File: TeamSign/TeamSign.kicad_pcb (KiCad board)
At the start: 2 copper layers, 241.2 x 139.8 mm, 203 parts, among them J1 RJ45, J2 Barrel_Jack_MountingPin, Q1 BSS138, Q2 BSS138, U1 TPS563200, U2 ESP32-Devkit_C_V4

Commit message: Added reset pins back in and broke out the pins in the team control area; should be easier now.  Yay!
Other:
- board size 241.2 x 139.8 mm -> 231.1 x 135.5 mm
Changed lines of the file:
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@@
       (net 1 "GND") (pintype "passive"))
   )
-  (gr_rect (start 32 19.25) (end 273.25 159)
-    (stroke (width 0.1) (type default)) (fill none) (layer "Edge.Cuts"))
+  (gr_line (start 258.15 154.725) (end 37 154.725)
+    (stroke (width 0.1) (type default)) (layer "Edge.Cuts"))
+  (gr_line (start 32 149.725) (end 32 24.25)
+    (stroke (width 0.1) (type default)) (layer "Edge.Cuts"))
+  (gr_line (start 263.15 24.25) (end 263.15 149.725)
+    (stroke (width 0.1) (type default)) (layer "Edge.Cuts"))
+  (gr_arc (start 32 24.25) (mid 33.464466 20.714466) (end 37 19.25)
+    (stroke (width 0.1) (type default)) (layer "Edge.Cuts"))
+  (gr_arc (start 263.15 149.725) (mid 261.685534 153.260534) (end 258.15 154.725)
+    (stroke (width 0.1) (type default)) (layer "Edge.Cuts"))
+  (gr_line (start 37 19.25) (end 258.15 19.25)
+    (stroke (width 0.1) (type default)) (layer "Edge.Cuts"))
+  (gr_arc (start 258.15 19.25) (mid 261.685534 20.714466) (end 263.15 24.25)
+    (stroke (width 0.1) (type default)) (layer "Edge.Cuts"))
+  (gr_arc (start 37 154.725) (mid 33.464466 153.260534) (end 32 149.725)
+    (stroke (width 0.1) (type default)) (layer "Edge.Cuts"))
   (gr_text "888" (at 30.9499 162.5346) (layer "F.SilkS")
     (effects (font (face "DSEG7 Classic Mini") (size 70 70) (thickness 0.3) bold) (justify left bottom))

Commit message: Added power area, and started drawing pours.
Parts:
- added C87: 100nF, Capacitor_SMD:C_1206_3216Metric_Pad1.33x1.80mm_HandSolder, F.Cu at (193.9, 26.3)
- added C90: 100nF, Capacitor_SMD:C_1206_3216Metric_Pad1.33x1.80mm_HandSolder, F.Cu at (208.2, 26.3)
- added C93: 100nF, Capacitor_SMD:C_1206_3216Metric_Pad1.33x1.80mm_HandSolder, F.Cu at (222.4, 26.3)
- added C96: 100nF, Capacitor_SMD:C_1206_3216Metric_Pad1.33x1.80mm_HandSolder, F.Cu at (179.7, 26.3)
- added D29: SK6812, LED_SMD:LED_SK6812_PLCC4_5.0x5.0mm_P3.2mm, F.Cu at (222.8, 33.0)
- added D30: SK6812, LED_SMD:LED_SK6812_PLCC4_5.0x5.0mm_P3.2mm, F.Cu at (208.4, 33.0)
- added D31: SK6812, LED_SMD:LED_SK6812_PLCC4_5.0x5.0mm_P3.2mm, F.Cu at (194.0, 33.0)
- added D32: SK6812, LED_SMD:LED_SK6812_PLCC4_5.0x5.0mm_P3.2mm, F.Cu at (179.6, 33.0)
- added H1: MountingHole, MountingHole:MountingHole_3.2mm_M3, F.Cu at (30.0, 20.0)
- added H2: MountingHole, MountingHole:MountingHole_3.2mm_M3, F.Cu at (260.0, 19.7)
- added H3: MountingHole, MountingHole:MountingHole_3.2mm_M3, F.Cu at (30.0, 155.0)
- added H4: MountingHole, MountingHole:MountingHole_3.2mm_M3, F.Cu at (260.0, 155.0)
- moved C998 31.2 mm to (131.6, 24.8), turned to 90 degrees
- moved C999 28.9 mm to (135.7, 24.8), turned to 90 degrees
- moved L1 27.4 mm to (152.6, 26.0)
- moved U1 25.2 mm to (143.8, 24.7)
- moved R4 23.6 mm to (68.4, 34.0), turned to 0 degrees
- moved R3 22.4 mm to (139.0, 24.8), turned to 90 degrees
- moved C899 19.6 mm to (148.7, 35.0), turned to 90 degrees
- moved R2 19.2 mm to (141.5, 30.6), turned to 180 degrees
- moved C799 17.9 mm to (146.0, 20.0)
- moved R6 16.8 mm to (57.8, 27.0), turned to 0 degrees
- moved R5 16.3 mm to (65.1, 38.0)
- moved J2 16.1 mm to (122.6, 28.8)
- moved R1 15.5 mm to (145.6, 29.4), turned to 90 degrees
- moved C898 15.1 mm to (155.8, 35.0), turned to 90 degrees
- moved Q2 13.4 mm to (57.7, 30.8)
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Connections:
- D92 pad 4: /LED Array 3/sk_output_pin -> /led_output_frontfiring
- U2 pad 26: /sk_input -> /stacklight_out
- U2 pad 27: /stacklight_out -> /sk_input
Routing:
- net +5V: track 0.00 -> 189.7 mm, vias 0 -> 5
- net +3.3V: track 0.00 -> 87.2 mm, vias 0 -> 4
- net /sk_lvl_shifted: track 0.00 -> 54.6 mm
- net /stacklight_lvl_shift: track 0.00 -> 49.4 mm
- net /stacklight_out: track 0.00 -> 45.4 mm
- net +12V: track 0.00 -> 21.7 mm
- net Net-(U1-EN): track 0.00 -> 14.2 mm, vias 0 -> 2
- net /sk_input: track 0.00 -> 12.5 mm
- net Net-(U1-VBST): track 0.00 -> 11.8 mm
- net Net-(U1-SW): track 0.00 -> 8.79 mm
- net Net-(U1-VFB): track 0.00 -> 7.12 mm
- net GND: track 0.00 -> 0.09 mm, vias 0 -> 53
- added copper zone on F.Cu, net +5V
- added copper zone on B.Cu, net GND
- added copper zone on F.Cu, net GND
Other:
- board size 231.1 x 135.5 mm -> 240 x 145 mm
- board text added: "locked"
- board text removed: "888"

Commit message: Fight with Freerouting, turns out there's a bug.  Routing by hand.
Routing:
- net +5V: track 189.7 -> 300.5 mm
- net /LED Array 1/sk_output_pin: track 0.00 -> 81.8 mm
- net /LED Array 2/sk_output_pin: track 0.00 -> 79.7 mm
- net /led_output_frontfiring: track 0.00 -> 78.8 mm, vias 0 -> 2
- net GND: track 0.09 -> 45.4 mm, vias 53 -> 61
- net +12V: track 21.7 -> 45.6 mm
- net Net-(D31-DOUT): track 0.00 -> 10.8 mm
- net Net-(D29-DOUT): track 0.00 -> 10.8 mm
- net Net-(D30-DOUT): track 0.00 -> 10.8 mm
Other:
- board text added: "888"
- board text removed: "locked"

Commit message: Mostly routed, needs side-firing cleanup.
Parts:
- moved C16 3.53 mm to (212.0, 139.8)
- turned C11 to 180 degrees
- turned C14 to 180 degrees
- turned C5 to 180 degrees
- turned C8 to 180 degrees
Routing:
- net +5V: track 300.5 -> 2683.5 mm, vias 5 -> 42
- net Net-(D24-DOUT): track 0.00 -> 59.0 mm
- net Net-(D60-DOUT): track 0.00 -> 56.7 mm
- net Net-(D88-DOUT): track 0.00 -> 54.9 mm
- net Net-(D304-DOUT): track 0.00 -> 25.5 mm, vias 0 -> 2
- net Net-(D305-DOUT): track 0.00 -> 25.2 mm
- net Net-(D302-DOUT): track 0.00 -> 24.5 mm, vias 0 -> 2
- net Net-(D303-DOUT): track 0.00 -> 22.8 mm, vias 0 -> 2
- net GND: track 45.4 -> 68.1 mm, vias 61 -> 194
- net Net-(D300-DOUT): track 0.00 -> 21.5 mm, vias 0 -> 2
- net Net-(D8-DOUT): track 0.00 -> 21.0 mm, vias 0 -> 2
- net Net-(D306-DOUT): track 0.00 -> 20.9 mm, vias 0 -> 2
- net Net-(D44-DOUT): track 0.00 -> 19.7 mm, vias 0 -> 2
- net Net-(D84-DOUT): track 0.00 -> 19.5 mm
- net Net-(D72-DOUT): track 0.00 -> 19.5 mm
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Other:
- board text added: "locked"
- board text removed: "888"

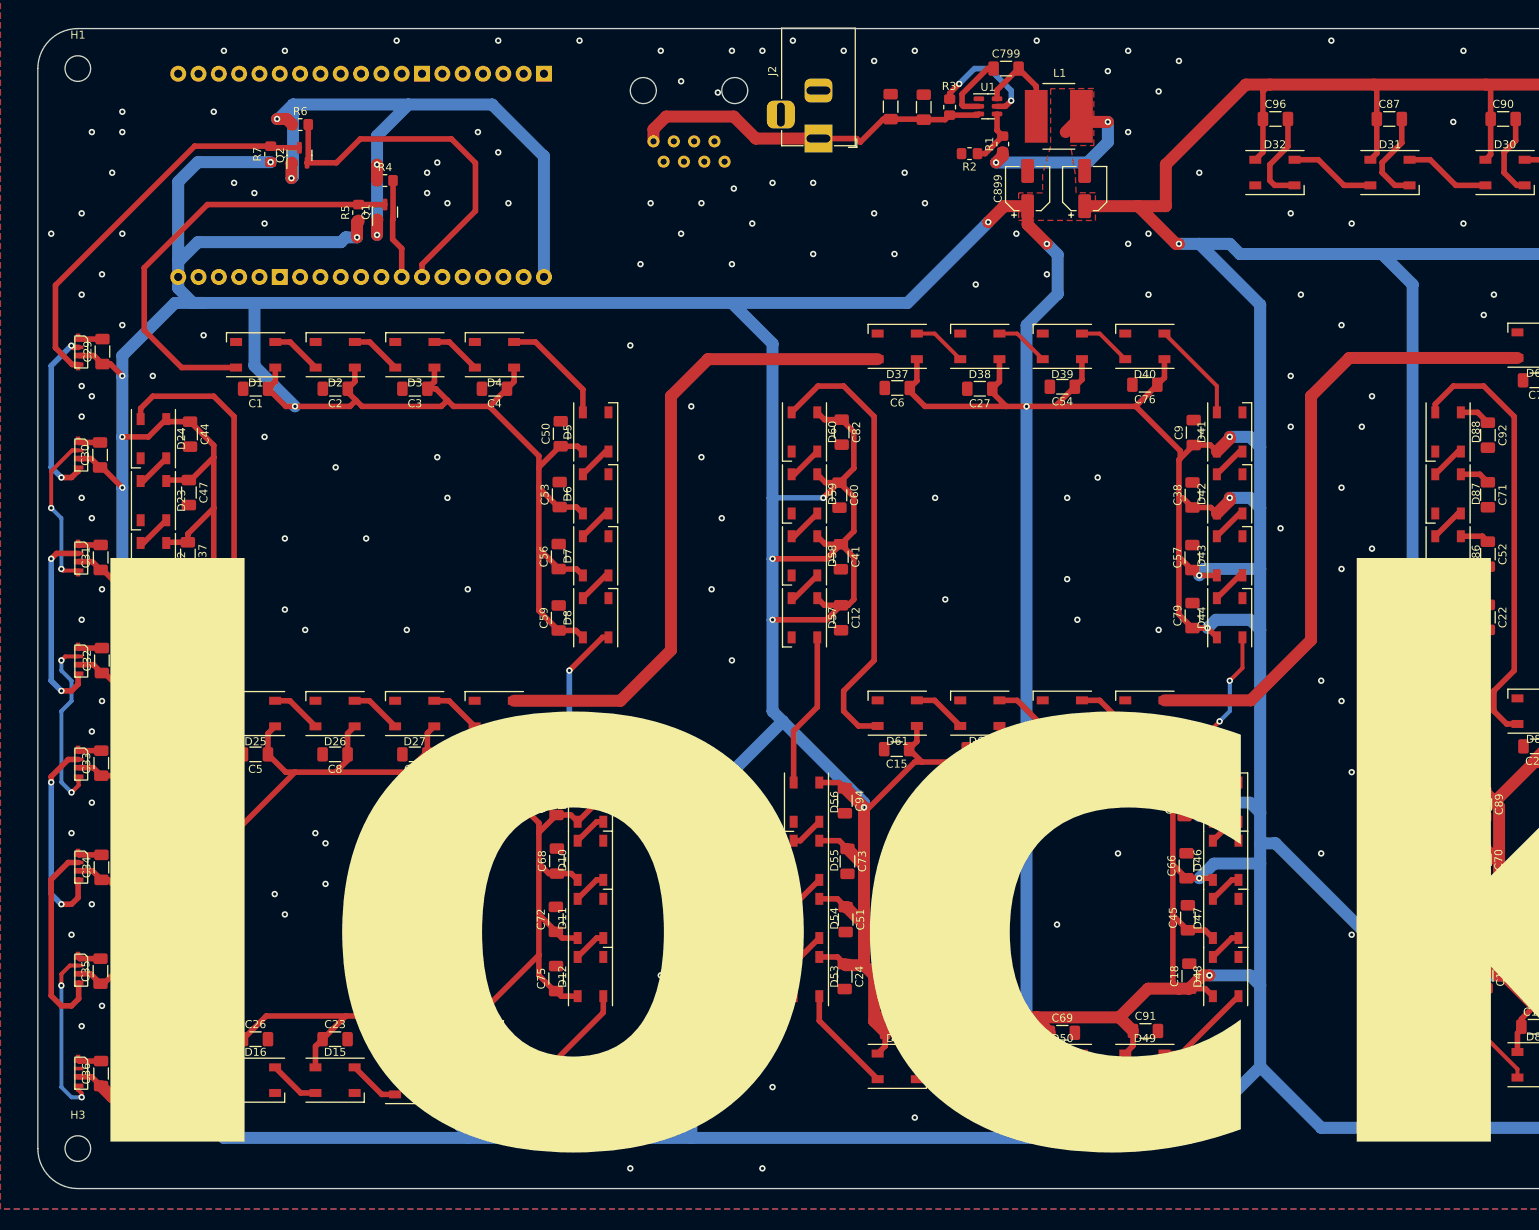
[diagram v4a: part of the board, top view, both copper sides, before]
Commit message: Changed thermal relief style, updated LEDs, seem to have worked?  idk, yay
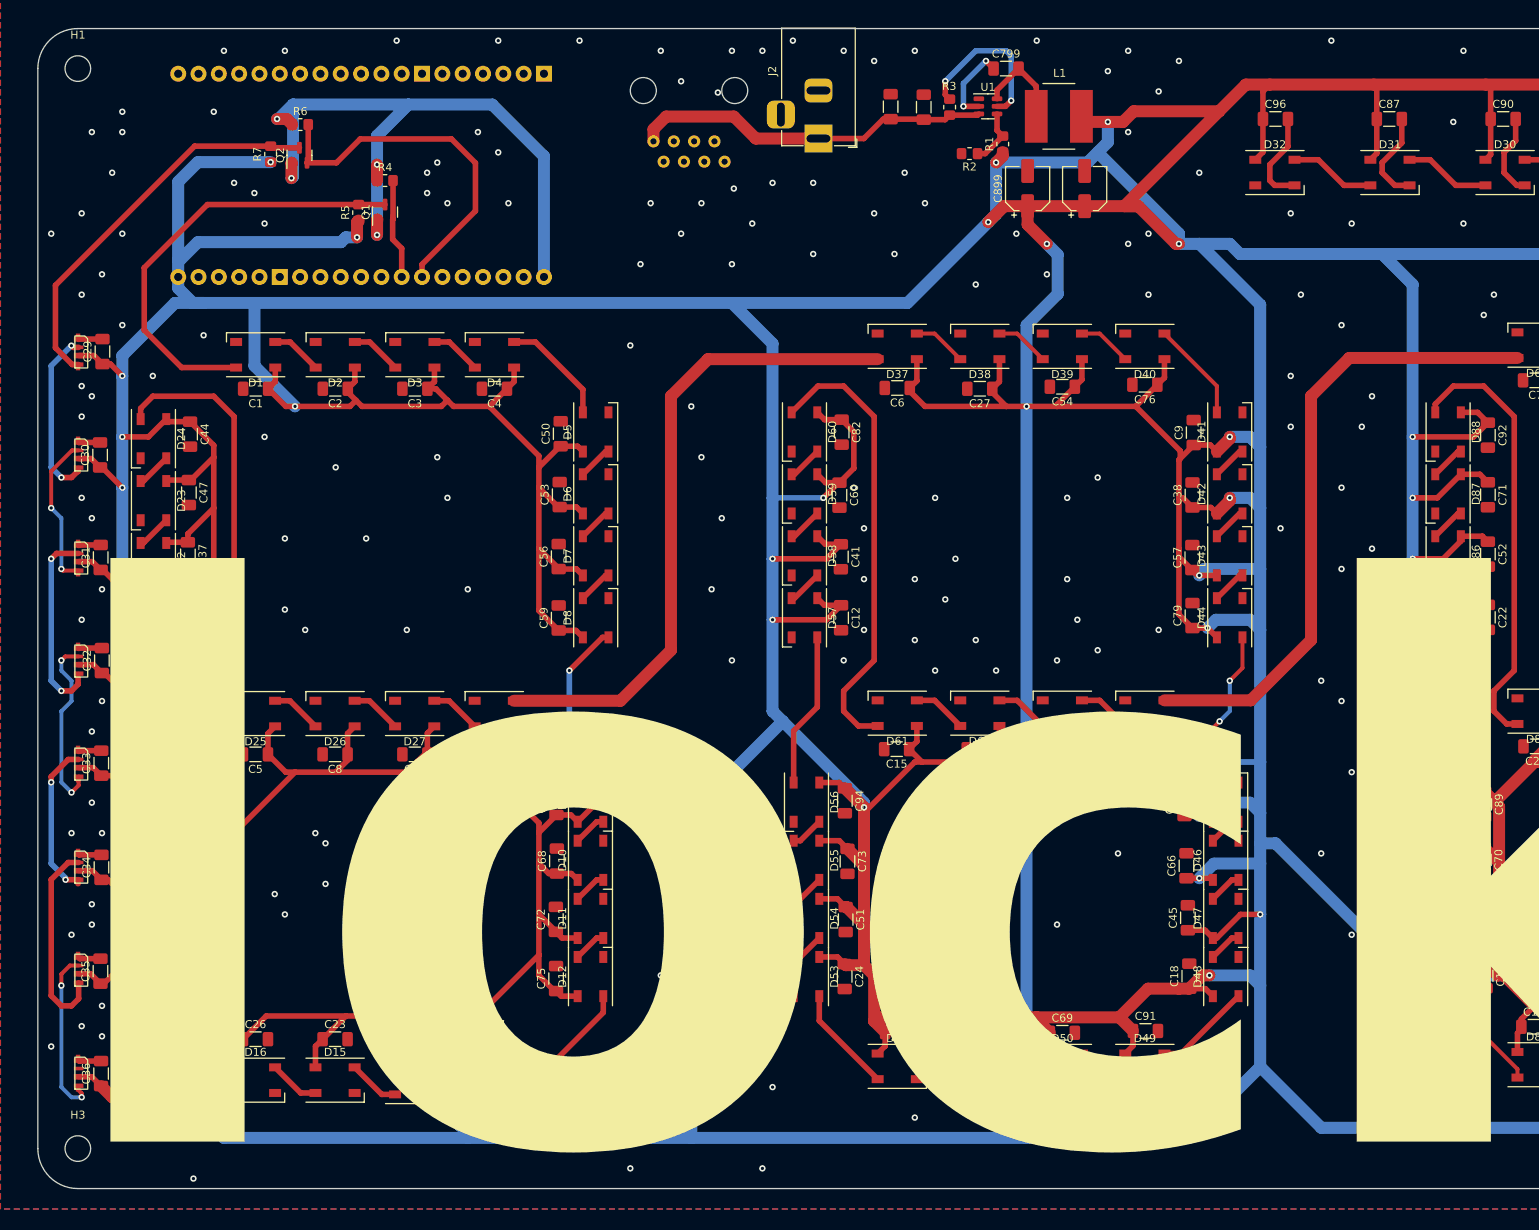
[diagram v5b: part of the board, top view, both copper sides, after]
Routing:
- net +5V: track 2683.5 -> 2722.5 mm, vias 42 -> 48
- net Net-(U1-EN): track 14.2 -> 20.2 mm
- net Net-(D304-DOUT): track 25.5 -> 20.1 mm
- net Net-(U1-SW): track 8.79 -> 10.1 mm, vias 0 -> 2
- net Net-(D303-DOUT): track 22.8 -> 23.3 mm
- net Net-(D300-DOUT): track 21.5 -> 22.0 mm
- net GND: vias 194 -> 223
- removed copper zone on F.Cu, net +5V

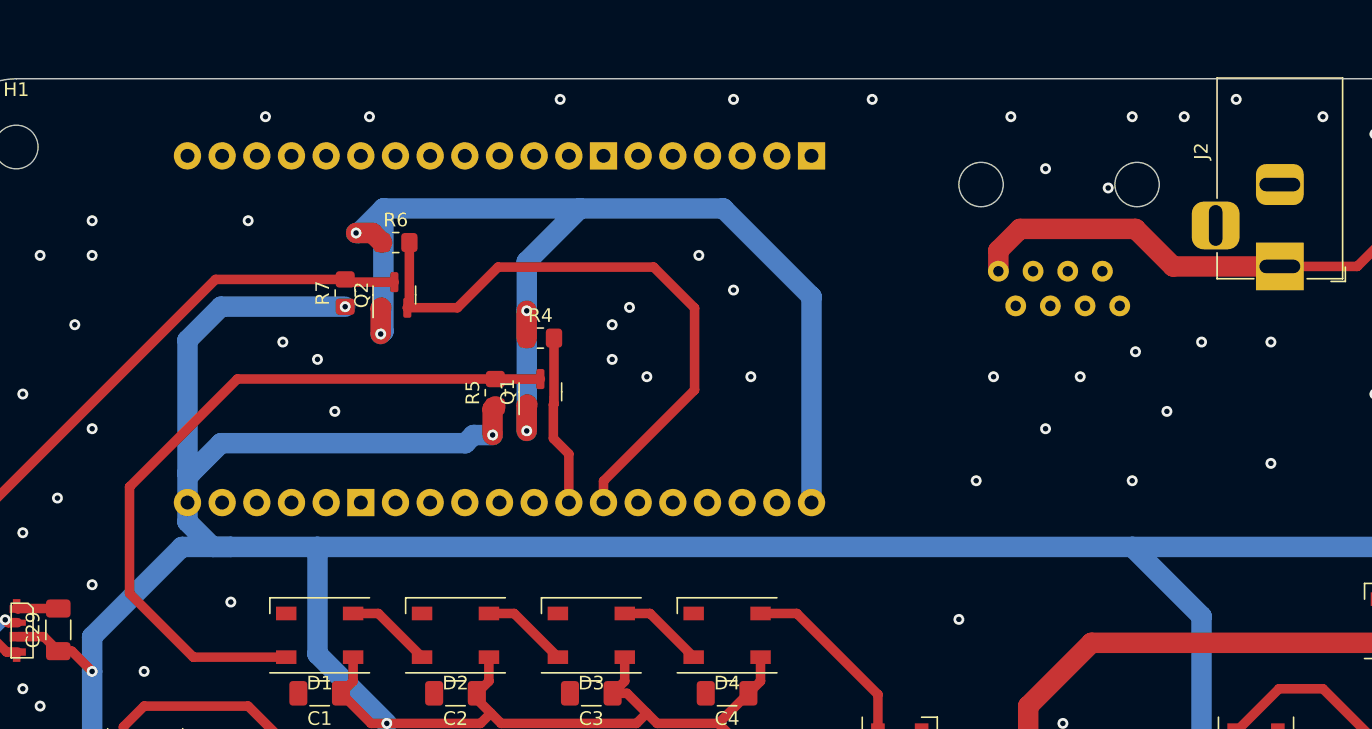
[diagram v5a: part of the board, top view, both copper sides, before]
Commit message: Move connectors to front of board so they're in the bulky area.
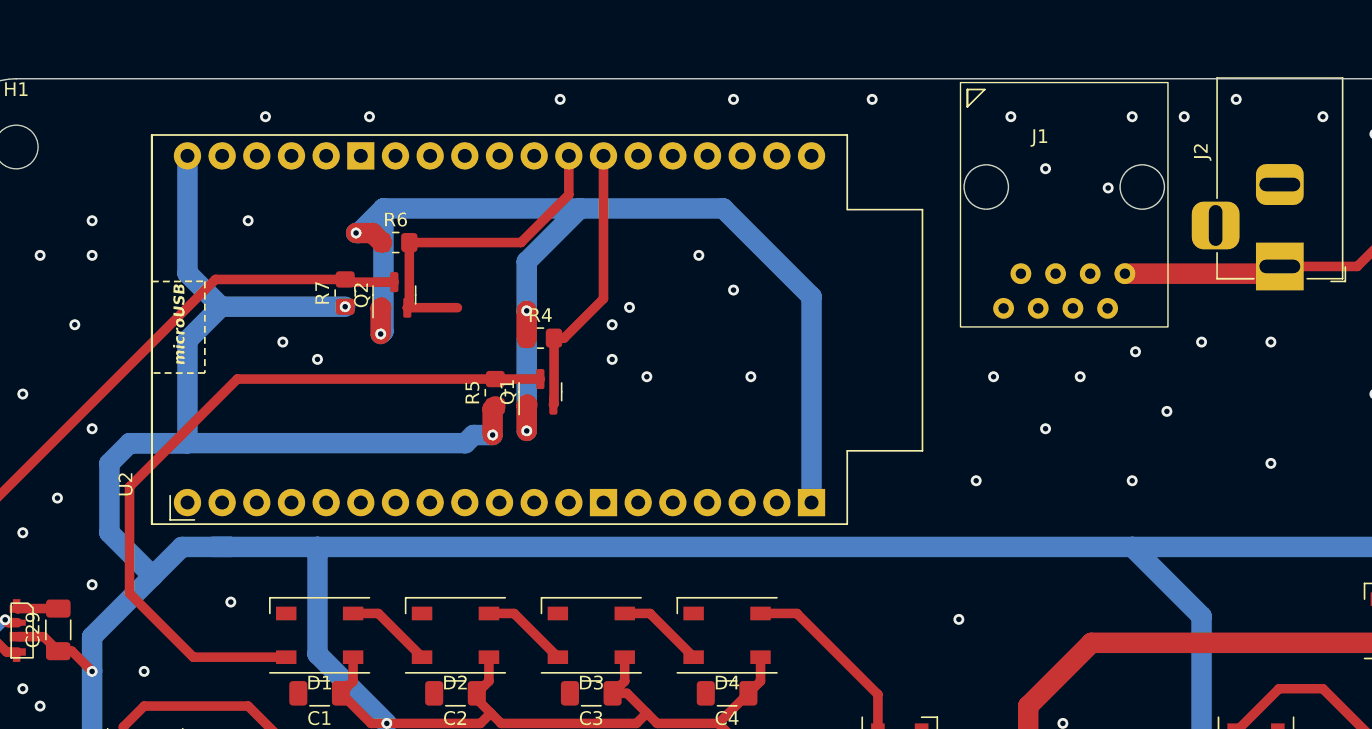
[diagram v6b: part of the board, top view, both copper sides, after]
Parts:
- J1, U2: moved to F.Cu
- moved J1 14.8 mm to (99.2, 15.3), turned to 0 degrees
- turned U2 to 90 degrees
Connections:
- U2 pad 26: /stacklight_out -> /sk_input
- U2 pad 27: /sk_input -> /stacklight_out
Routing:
- net +5V: track 2722.5 -> 2745.4 mm
- net /stacklight_out: track 45.4 -> 24.5 mm
- net +12V: track 45.2 -> 32.9 mm
- net /sk_input: track 12.5 -> 20.2 mm
- net GND: vias 223 -> 222
